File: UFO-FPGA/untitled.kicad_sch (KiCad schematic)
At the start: 3 parts, among them U4 MC34063AD

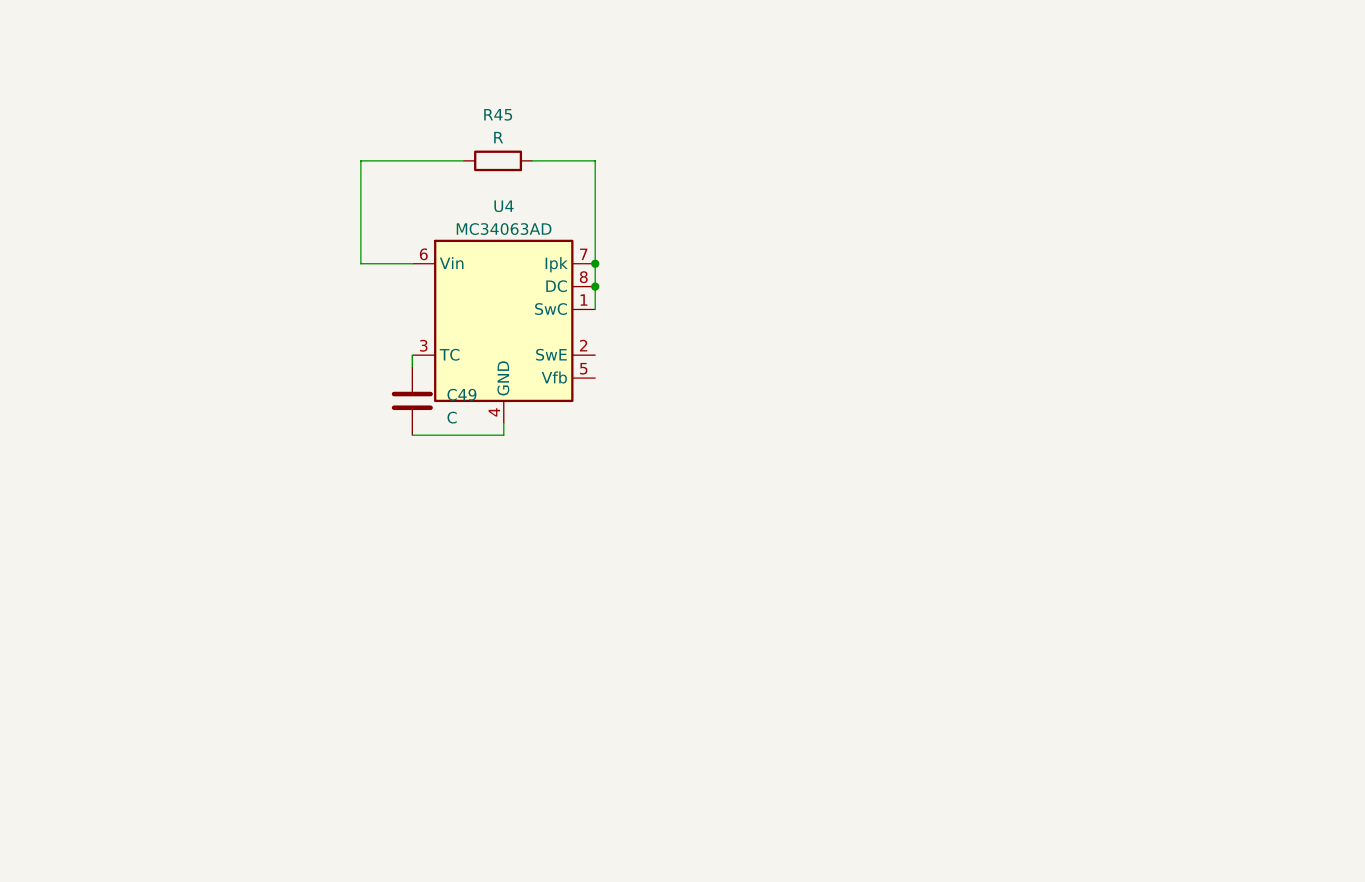
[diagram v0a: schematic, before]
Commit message: De inverting supply schakeling gemaakt
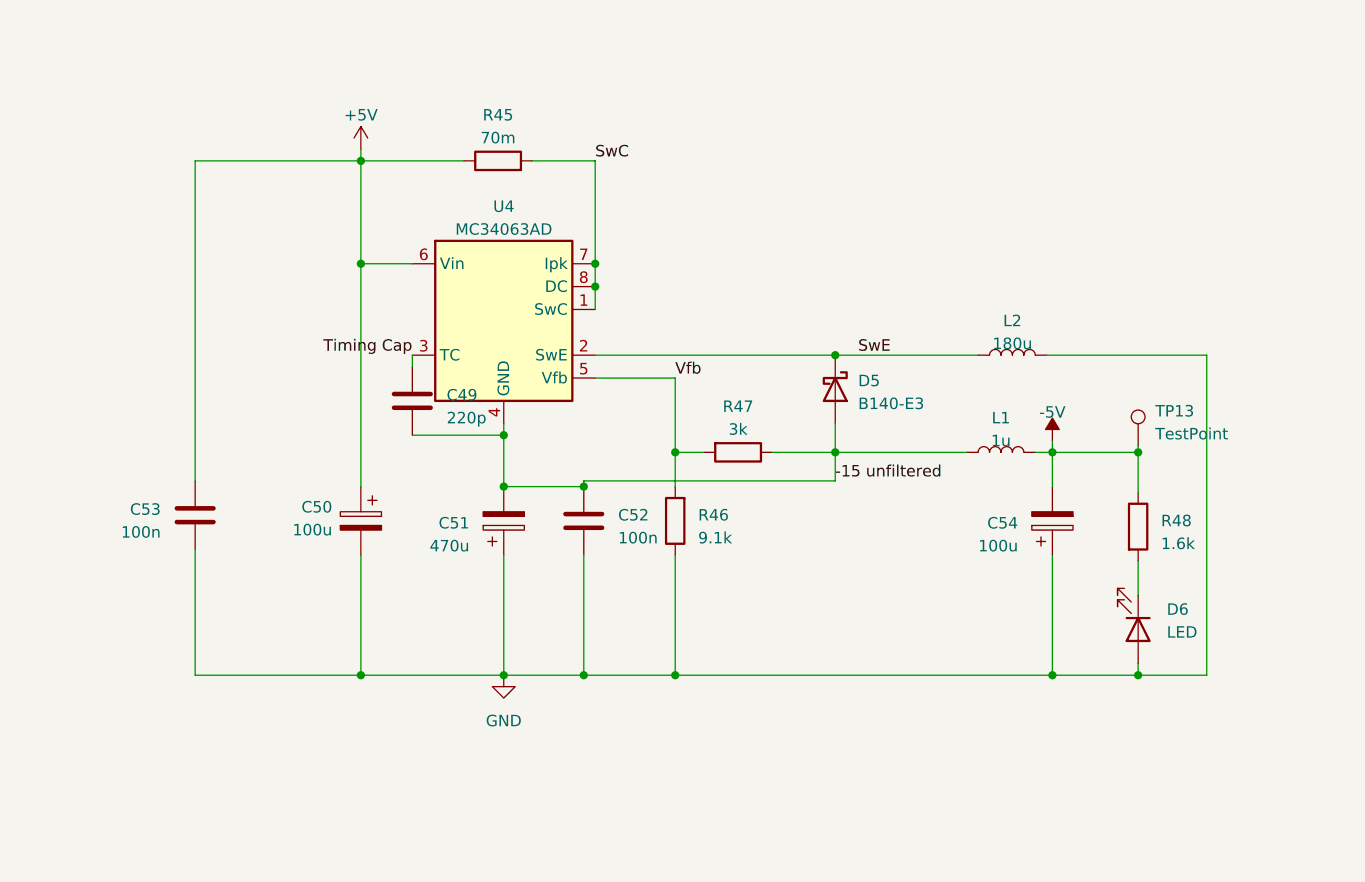
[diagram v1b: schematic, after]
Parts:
- added C50, C54: 100u, symbol Device:C_Polarized
- added C51: 470u, symbol Device:C_Polarized
- added C52, C53: 100n, symbol Device:C
- added D5: B140-E3, Diode_SMD:D_SMA, symbol Diode:B140-E3
- added D6: LED, symbol Device:LED
- added L1: 1u, symbol Device:L
- added L2: 180u, symbol Device:L
- added R46: 9.1k, symbol Device:R
- added R47: 3k, symbol Device:R
- added R48: 1.6k, symbol Device:R
- added TP13: TestPoint, symbol Connector:TestPoint
- C49: value C -> 220p
- R45: value R -> 70m
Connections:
- net +5V: now reaches R45.1, U4.6 (Vin)
- net +5V: now also C50.1, C53.1
- net SwC: now reaches R45.2, U4.1 (SwC), U4.7 (Ipk), U4.8 (DC)
- net SwE: now reaches U4.2 (SwE)
- net SwE: now also D5.1 (K), L2.1
- net Timing Cap: now reaches C49.1, U4.3 (TC)
- net -15 unfiltered: now reaches C49.2, U4.4 (GND)
- net -15 unfiltered: now also C51.2, C52.1, D5.2 (A), L1.1, R47.1
- net Vfb: now reaches U4.5 (Vfb)
- net Vfb: now also R46.2, R47.2
- new net: D6.1 (K), R48.2
- new net -5V: C54.2, L1.2, R48.1, TP13.1
- new net GND: C50.2, C51.1, C52.2, C53.2, C54.1, D6.2 (A), L2.2, R46.1

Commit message: Opamp gemaakt van de ADC
Enkel nog begrijpen wat VDC is. Aan docent vragen?
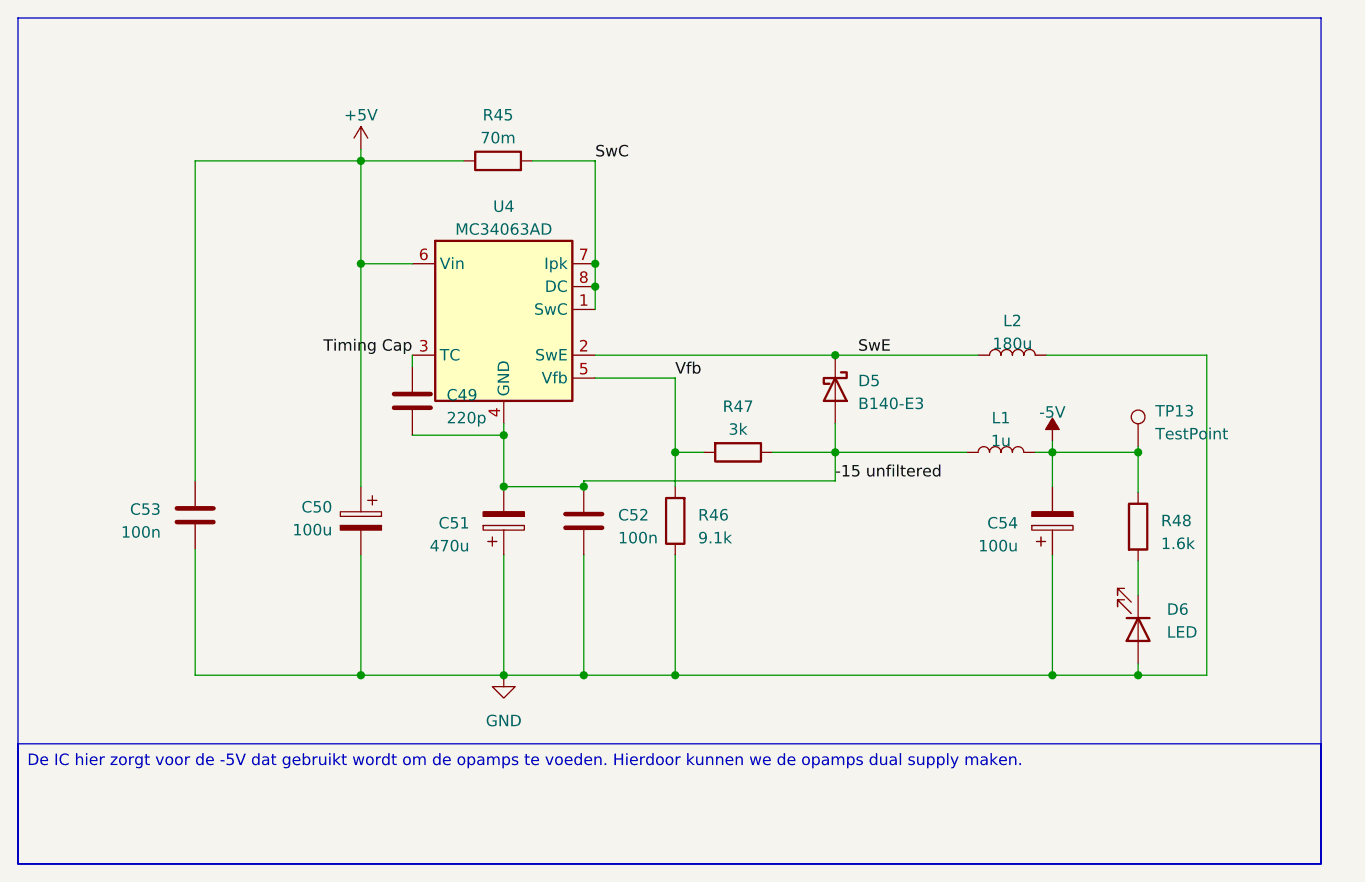
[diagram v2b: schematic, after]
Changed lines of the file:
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@@
     (stroke (width 0) (type default))
+  )
+  (rectangle (start 78.105 52.705) (end 222.885 146.685)
+    (stroke (width 0) (type default))
+    (fill (type none))
+  )
+  (text_box "De IC hier zorgt voor de -5V dat gebruikt wordt om de opamps te voeden. Hierdoor kunnen we de opamps dual supply maken."
+    (at 78.105 133.35 0) (size 144.78 13.335)
+    (stroke (width 0) (type default))
+    (fill (type none))
+    (effects (font (size 1.27 1.27)) (justify left top))
   )
   (label "-15 unfiltered" (at 168.91 104.14 0) (fields_autoplaced)

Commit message: Revision
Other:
- company: (none) -> Universal-Field-Objects
- title: (none) -> Invert-5V-Dual-Ramp
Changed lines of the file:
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@@
 (kicad_sch (version 20230121) (generator eeschema)
   (paper "A4")
+  (title_block
+    (title "Invert-5V-Dual-Ramp")
+    (date "2023-04-25")
+    (rev "V0.5")
+    (company "Universal-Field-Objects")
+  )
   (junction (at 140.97 125.73) (diameter 0) (color 0 0 0 0)
   )

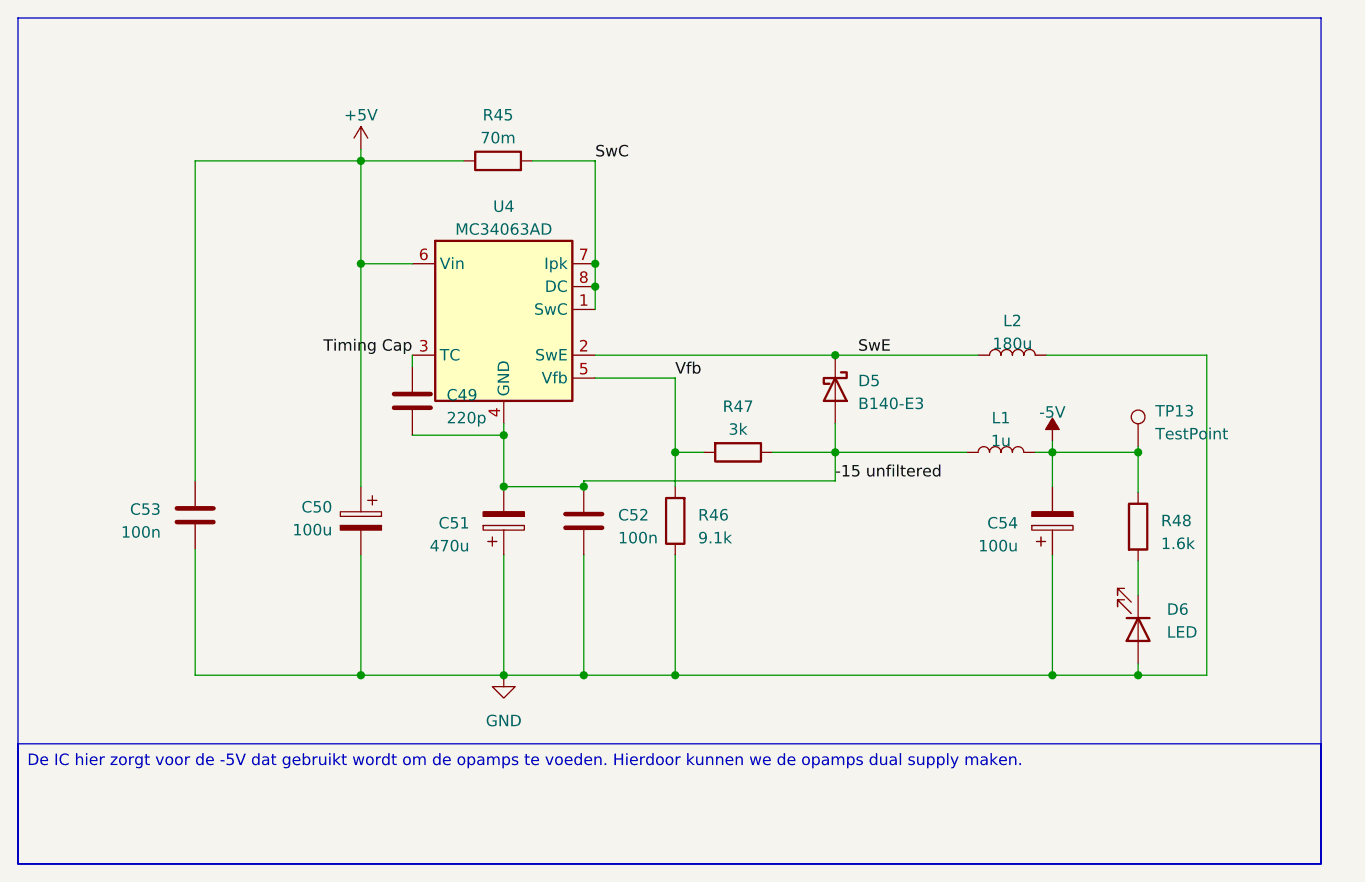
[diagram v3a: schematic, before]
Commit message: PCB and footprint
Added foorprints and moved on pcb layout
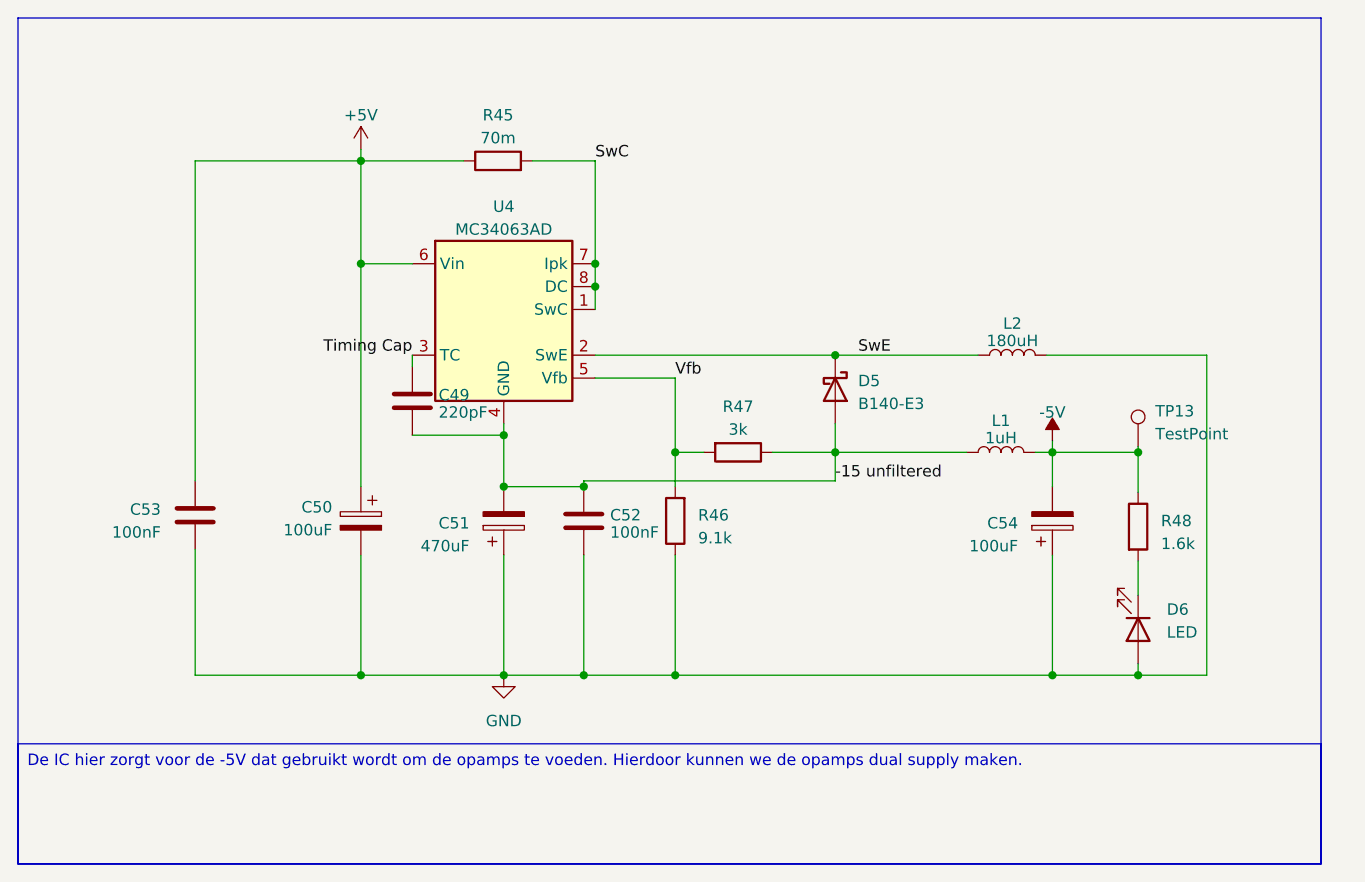
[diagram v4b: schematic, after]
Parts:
- C49: value 220p -> 220pF
- C50, C54: value 100u -> 100uF
- C51: value 470u -> 470uF
- C52, C53: value 100n -> 100nF
- L1: value 1u -> 1uH
- L2: value 180u -> 180uH
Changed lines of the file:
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@@
       (effects (font (size 1.27 1.27)) (justify left))
     )
-    (property "Value" "100n" (at 93.98 109.855 0)
+    (property "Value" "100nF" (at 93.98 109.855 0)
       (effects (font (size 1.27 1.27)) (justify left))
     )
@@
       (effects (font (size 1.27 1.27)) (justify right))
     )
-    (property "Value" "470u" (at 128.27 111.379 0)
+    (property "Value" "470uF" (at 128.27 111.379 0)
       (effects (font (size 1.27 1.27)) (justify right))
     )
@@
   (symbol (lib_id "Device:C") (at 140.97 108.585 0) (unit 1)
     (in_bom yes) (on_board yes) (dnp no) (fields_autoplaced)
-    (property "Reference" "C52" (at 144.78 107.95 0)
-      (effects (font (size 1.27 1.27)) (justify left))
-    )
-    (property "Value" "100n" (at 144.78 110.49 0)
+    (property "Reference" "C52" (at 143.891 107.9413 0)
+      (effects (font (size 1.27 1.27)) (justify left))
+    )
+    (property "Value" "100nF" (at 143.891 109.8623 0)
       (effects (font (size 1.27 1.27)) (justify left))
     )
@@
   (symbol (lib_id "Device:C") (at 121.92 95.25 0) (unit 1)
     (in_bom yes) (on_board yes) (dnp no) (fields_autoplaced)
-    (property "Reference" "C49" (at 125.73 94.615 0)
-      (effects (font (size 1.27 1.27)) (justify left))
-    )
-    (property "Value" "220p" (at 125.73 97.155 0)
+    (property "Reference" "C49" (at 124.841 94.6063 0)
+      (effects (font (size 1.27 1.27)) (justify left))
+    )
+    (property "Value" "220pF" (at 124.841 96.5273 0)
       (effects (font (size 1.27 1.27)) (justify left))
     )
@@
       (effects (font (size 1.27 1.27)) (justify right))
     )
-    (property "Value" "100u" (at 189.23 111.379 0)
+    (property "Value" "100uF" (at 189.23 111.379 0)
       (effects (font (size 1.27 1.27)) (justify right))
     )
@@
   (symbol (lib_id "Device:L") (at 188.595 90.17 90) (unit 1)
     (in_bom yes) (on_board yes) (dnp no) (fields_autoplaced)
-    (property "Reference" "L2" (at 188.595 86.36 90)
-      (effects (font (size 1.27 1.27)))
-    )
-    (property "Value" "180u" (at 188.595 88.9 90)
+    (property "Reference" "L2" (at 188.595 86.6547 90)
+      (effects (font (size 1.27 1.27)))
+    )
+    (property "Value" "180uH" (at 188.595 88.5757 90)
       (effects (font (size 1.27 1.27)))
     )
@@
   (symbol (lib_id "Device:L") (at 187.325 100.965 90) (unit 1)
     (in_bom yes) (on_board yes) (dnp no) (fields_autoplaced)
-    (property "Reference" "L1" (at 187.325 97.155 90)
-      (effects (font (size 1.27 1.27)))
-    )
-    (property "Value" "1u" (at 187.325 99.695 90)
+    (property "Reference" "L1" (at 187.325 97.4497 90)
+      (effects (font (size 1.27 1.27)))
+    )
+    (property "Value" "1uH" (at 187.325 99.3707 90)
       (effects (font (size 1.27 1.27)))
     )
@@
       (effects (font (size 1.27 1.27)) (justify left))
     )
-    (property "Value" "100u" (at 113.03 109.601 0)
-      (effects (font (size 1.27 1.27)) (justify left))
-    )
+    (property "Value" "100uF" (at 113.03 109.601 0)
+      (effects (font (size 1.27 1.27)) (justify left))
+    )

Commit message: footprints and PCB
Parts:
- D6: footprint (none) -> LED_SMD:LED_0805_2012Metric_Pad1.15x1.40mm_HandSolder
- TP13: footprint (none) -> TestPoint:TestPoint_Keystone_5000-5004_Miniature
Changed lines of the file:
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@@
       (effects (font (size 1.27 1.27)) (justify left))
     )
-    (property "Footprint" "" (at 207.645 100.33 0)
+    (property "Footprint" "TestPoint:TestPoint_Keystone_5000-5004_Miniature" (at 207.645 100.33 0)
       (effects (font (size 1.27 1.27)) hide)
     )
@@
       (effects (font (size 1.27 1.27)) (justify left))
     )
-    (property "Footprint" "" (at 202.565 120.65 0)
+    (property "Footprint" "LED_SMD:LED_0805_2012Metric_Pad1.15x1.40mm_HandSolder" (at 202.565 120.65 0)
       (effects (font (size 1.27 1.27)) hide)
     )

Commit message: footprint
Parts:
- C49, C52, C53: footprint (none) -> Capacitor_SMD:C_0805_2012Metric_Pad1.18x1.45mm_HandSolder
- R45, R46, R47, R48: footprint (none) -> Resistor_SMD:R_0805_2012Metric
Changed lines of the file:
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@@
       (effects (font (size 1.27 1.27)) (justify right))
     )
-    (property "Footprint" "" (at 152.908 108.585 90)
+    (property "Footprint" "Resistor_SMD:R_0805_2012Metric" (at 152.908 108.585 90)
       (effects (font (size 1.27 1.27)) hide)
     )
@@
       (effects (font (size 1.27 1.27)) (justify left))
     )
-    (property "Footprint" "" (at 96.8248 111.76 0)
+    (property "Footprint" "Capacitor_SMD:C_0805_2012Metric_Pad1.18x1.45mm_HandSolder" (at 96.8248 111.76 0)
       (effects (font (size 1.27 1.27)) hide)
     )
@@
       (effects (font (size 1.27 1.27)))
     )
-    (property "Footprint" "" (at 131.445 70.358 90)
+    (property "Footprint" "Resistor_SMD:R_0805_2012Metric" (at 131.445 70.358 90)
       (effects (font (size 1.27 1.27)) hide)
     )
@@
       (effects (font (size 1.27 1.27)) (justify left))
     )
-    (property "Footprint" "" (at 141.9352 112.395 0)
+    (property "Footprint" "Capacitor_SMD:C_0805_2012Metric_Pad1.18x1.45mm_HandSolder" (at 141.9352 112.395 0)
       (effects (font (size 1.27 1.27)) hide)
     )
@@
       (effects (font (size 1.27 1.27)))
     )
-    (property "Footprint" "" (at 158.115 99.187 90)
+    (property "Footprint" "Resistor_SMD:R_0805_2012Metric" (at 158.115 99.187 90)
       (effects (font (size 1.27 1.27)) hide)
     )
@@
       (effects (font (size 1.27 1.27)) (justify left))
     )
-    (property "Footprint" "" (at 122.8852 99.06 0)
+    (property "Footprint" "Capacitor_SMD:C_0805_2012Metric_Pad1.18x1.45mm_HandSolder" (at 122.8852 99.06 0)
       (effects (font (size 1.27 1.27)) hide)
     )
@@
       (effects (font (size 1.27 1.27)) (justify left))
     )
-    (property "Footprint" "" (at 200.787 109.22 90)
-      (effects (font (size 1.27 1.27)) hide)
-    )
+    (property "Footprint" "Resistor_SMD:R_0805_2012Metric" (at 200.787 109.22 90)
+      (effects (font (size 1.27 1.27)) hide)
+    )
